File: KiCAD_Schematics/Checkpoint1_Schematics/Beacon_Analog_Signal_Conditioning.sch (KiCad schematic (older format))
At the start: 19 parts, among them Q1 Photo_NPN, U1 MCP6294, U1 MCP6546, U4 MCP6294

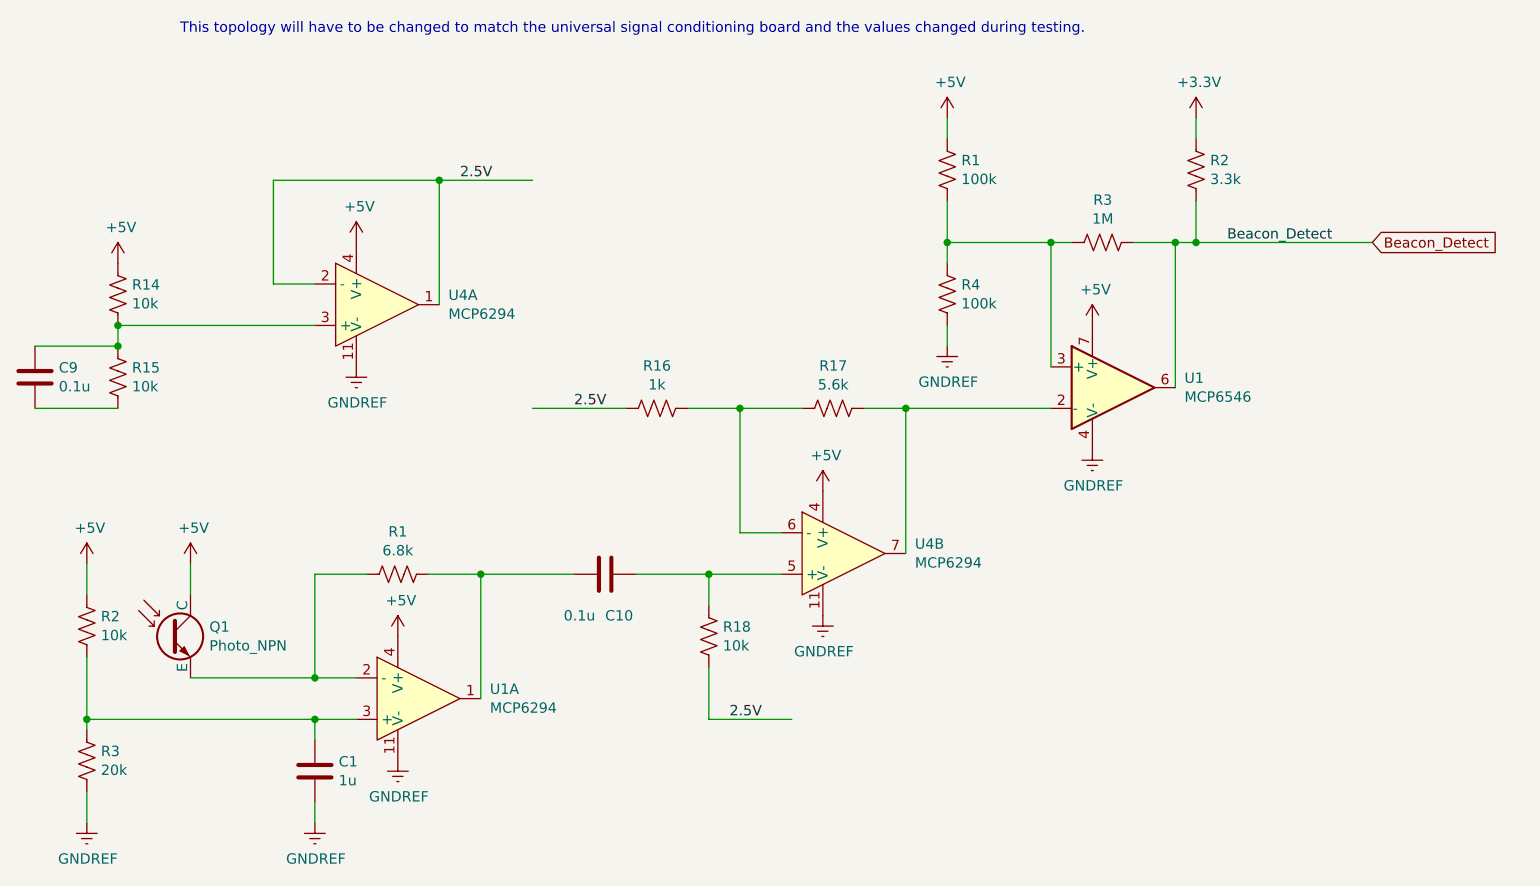
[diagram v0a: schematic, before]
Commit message: Update KiCAD schematic
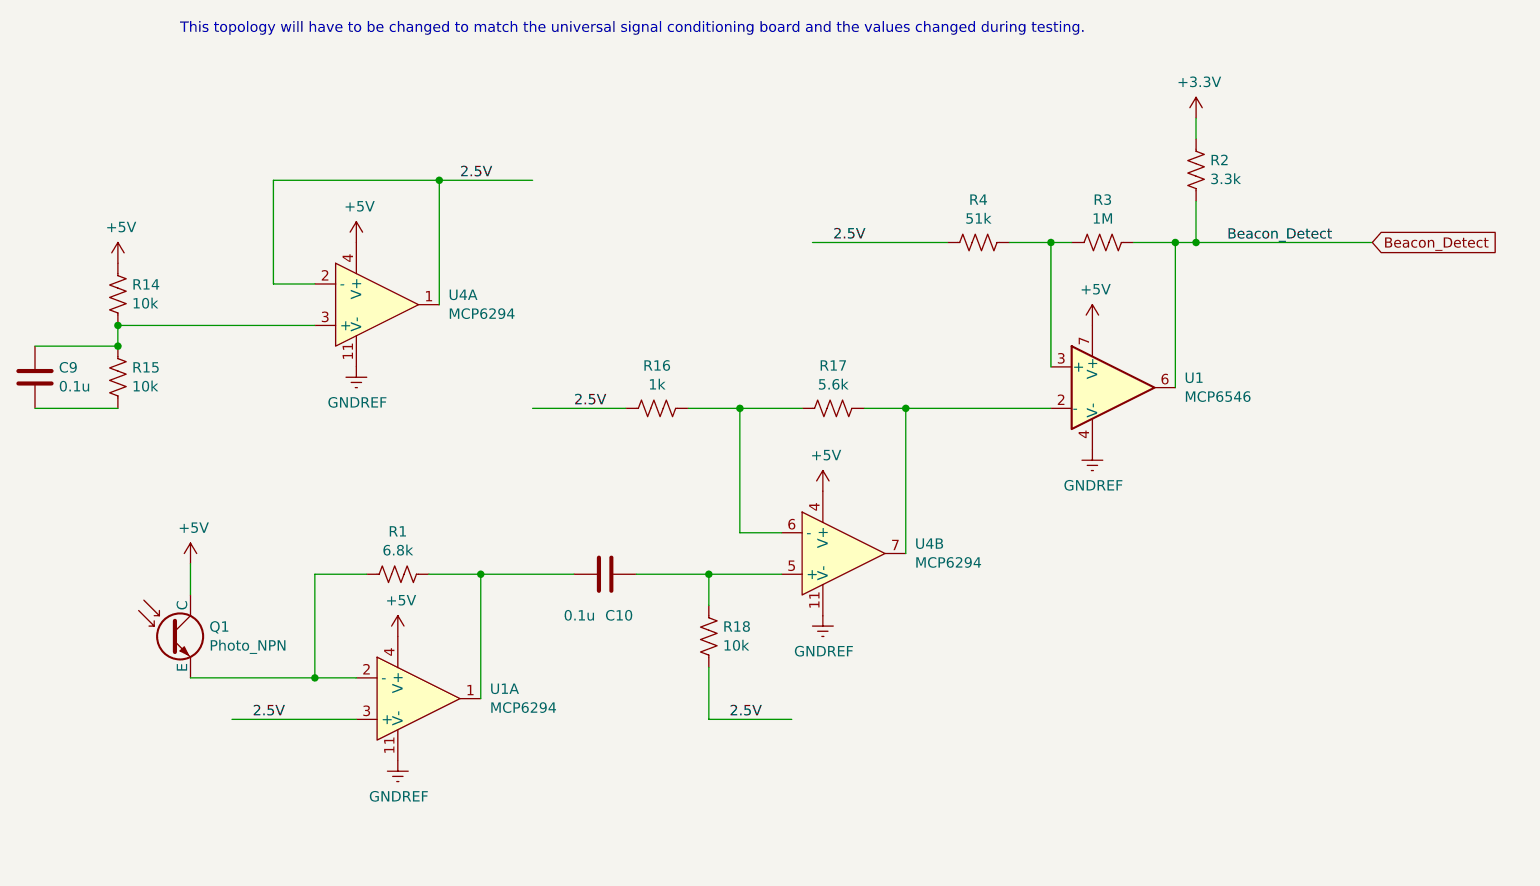
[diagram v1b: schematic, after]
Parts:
- removed C1: 1u, symbol ME218_BaseLib:Cap
- removed R1: 100k, symbol ME218_BaseLib:Res1
- removed R2: 10k, symbol ME218_BaseLib:Res1
- removed R3: 20k, symbol ME218_BaseLib:Res1
- R4: value 100k -> 51k
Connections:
- wire segments 51 -> 41
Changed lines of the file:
@@
 $Descr A4 11693 8268
 encoding utf-8
-Sheet 4 7
+Sheet 1 1
 Title "ME 218b Team 3 Project Schematic"
 Date ""
@@
 	1    0    0    -1
 $EndComp
-$Comp
-L power:+5V #PWR038
-U 1 1 61E4D0CB
-P 7100 2650
-F 0 "#PWR038" H 7100 2500 50  0001 C CNN
-F 1 "+5V" H 7115 2823 50  0000 C CNN
-F 2 "" H 7100 2650 50  0001 C CNN
-F 3 "" H 7100 2650 50  0001 C CNN
-	1    7100 2650
-	1    0    0    -1
-$EndComp
 Wire Wire Line
 	8000 3250 8200 3250
 Wire Wire Line
 	7600 3250 7700 3250
-Connection ~ 7600 3250
 Wire Wire Line
 	7600 3850 7600 3250
-Wire Wire Line
-	7100 3250 7100 3350
-Connection ~ 7100 3250
-Wire Wire Line
-	7100 3250 7600 3250
-Wire Wire Line
-	7100 3650 7100 3750
-Wire Wire Line
-	7100 3050 7100 3250
-Wire Wire Line
-	7100 2650 7100 2750
-$Comp
-L ME218_BaseLib:Res1 R4
-U 1 1 623811DC
-P 7100 3500
-F 0 "R4" H 7168 3546 50  0000 L CNN
-F 1 "100k" H 7168 3455 50  0000 L CNN
-F 2 "" V 7140 3490 50  0001 C CNN
-F 3 "" H 7100 3500 50  0001 C CNN
-	1    7100 3500
-	1    0    0    -1
-$EndComp
-$Comp
-L ME218_BaseLib:Res1 R1
-U 1 1 623811DB
-P 7100 2900
-F 0 "R1" H 7168 2946 50  0000 L CNN
-F 1 "100k" H 7168 2855 50  0000 L CNN
-F 2 "" V 7140 2890 50  0001 C CNN
-F 3 "" H 7100 2900 50  0001 C CNN
-	1    7100 2900
-	1    0    0    -1
-$EndComp
 $Comp
 L ME218_BaseLib:Res1 R3
@@
 $EndComp
 Wire Wire Line
-	4050 5550 4250 5550
-Connection ~ 4050 5550
-Wire Wire Line
-	4050 5650 4050 5550
-Wire Wire Line
-	4050 6050 4050 5950
-$Comp
-L ME218_BaseLib:Cap C1
-U 1 1 623811D4
-P 4050 5800
-F 0 "C1" H 4165 5846 50  0000 L CNN
-F 1 "1u" H 4165 5755 50  0000 L CNN
-F 2 "" H 4088 5650 50  0001 C CNN
-F 3 "" H 4050 5800 50  0001 C CNN
-	1    4050 5800
-	1    0    0    -1
-$EndComp
-Wire Wire Line
-	2950 5550 2950 5250
-Connection ~ 2950 5550
-Wire Wire Line
-	2950 5550 4050 5550
-Wire Wire Line
-	2950 5600 2950 5550
-Wire Wire Line
-	2950 5900 2950 6050
-Wire Wire Line
-	2950 4800 2950 4950
-$Comp
-L ME218_BaseLib:Res1 R3
-U 1 1 61DD96B1
-P 2950 5750
-F 0 "R3" H 3018 5796 50  0000 L CNN
-F 1 "20k" H 3018 5705 50  0000 L CNN
-F 2 "" V 2990 5740 50  0001 C CNN
-F 3 "" H 2950 5750 50  0001 C CNN
-	1    2950 5750
-	1    0    0    -1
-$EndComp
-$Comp
-L ME218_BaseLib:Res1 R2
-U 1 1 623811D2
-P 2950 5100
-F 0 "R2" H 3018 5146 50  0000 L CNN
-F 1 "10k" H 3018 5055 50  0000 L CNN
-F 2 "" V 2990 5090 50  0001 C CNN
-F 3 "" H 2950 5100 50  0001 C CNN
-	1    2950 5100
-	1    0    0    -1
-$EndComp
-$Comp
-L power:+5V #PWR01
-U 1 1 623811D0
-P 2950 4800
-F 0 "#PWR01" H 2950 4650 50  0001 C CNN
-F 1 "+5V" H 2965 4973 50  0000 C CNN
-F 2 "" H 2950 4800 50  0001 C CNN
-F 3 "" H 2950 4800 50  0001 C CNN
-	1    2950 4800
-	1    0    0    -1
-$EndComp
-Wire Wire Line
 	4600 4850 4850 4850
 Wire Wire Line
@@
 $EndComp
 $Comp
+L ME218_BaseLib:Photo_NPN Q1
+U 1 1 6238256B
+P 3350 5150
+F 0 "Q1" H 3541 5196 50  0000 L CNN
+F 1 "Photo_NPN" H 3541 5105 50  0000 L CNN
+F 2 "" H 3550 5250 50  0001 C CNN
+F 3 "" H 3350 5150 50  0001 C CNN
+	1    3350 5150
+	1    0    0    -1
+$EndComp
+$Comp
+L power:+5V #PWR02
+U 1 1 6238256A
+P 3450 4800
+F 0 "#PWR02" H 3450 4650 50  0001 C CNN
+F 1 "+5V" H 3465 4973 50  0000 C CNN
+F 2 "" H 3450 4800 50  0001 C CNN
+F 3 "" H 3450 4800 50  0001 C CNN
+	1    3450 4800
+	1    0    0    -1
+$EndComp
+Connection ~ 8300 3250
+Wire Wire Line
+	8300 3250 9150 3250
+Text Label 8450 3250 0    49   ~ 0
+Beacon_Detect
+Text GLabel 9150 3250 2    49   Input ~ 0
+Beacon_Detect
+Text Notes 3400 2250 0    50   ~ 0
+This topology will have to be changed to match the universal signal conditioning board and the values changed during testing.
+$Comp
+L power:GNDREF #PWR046
+U 1 1 623EC563
+P 4450 5750
+F 0 "#PWR046" H 4450 5500 50  0001 C CNN
+F 1 "GNDREF" H 4455 5577 50  0000 C CNN
+F 2 "" H 4450 5750 50  0001 C CNN
+F 3 "" H 4450 5750 50  0001 C CNN
+	1    4450 5750
+	1    0    0    -1
+$EndComp
+$Comp
+L power:GNDREF #PWR045
+U 1 1 623EC85B
+P 6500 5050
+F 0 "#PWR045" H 6500 4800 50  0001 C CNN
+F 1 "GNDREF" H 6505 4877 50  0000 C CNN
+F 2 "" H 6500 5050 50  0001 C CNN
+F 3 "" H 6500 5050 50  0001 C CNN
+	1    6500 5050
+	1    0    0    -1
+$EndComp
+$Comp
+L power:GNDREF #PWR043
+U 1 1 623ED00D
+P 7800 4250
+F 0 "#PWR043" H 7800 4000 50  0001 C CNN
+F 1 "GNDREF" H 7805 4077 50  0000 C CNN
+F 2 "" H 7800 4250 50  0001 C CNN
+F 3 "" H 7800 4250 50  0001 C CNN
+	1    7800 4250
+	1    0    0    -1
+$EndComp
+$Comp
+L power:GNDREF #PWR042
+U 1 1 623EEBCB
+P 4250 3850
+F 0 "#PWR042" H 4250 3600 50  0001 C CNN
+F 1 "GNDREF" H 4255 3677 50  0000 C CNN
+F 2 "" H 4250 3850 50  0001 C CNN
+F 3 "" H 4250 3850 50  0001 C CNN
+	1    4250 3850
+	1    0    0    -1
+$EndComp
+Text Label 6550 3250 0    50   ~ 0
+2.5V
+$Comp
+L ME218_BaseLib:Res1 R4
+U 1 1 6212ADA5
+P 7250 3250
+F 0 "R4" V 7045 3250 50  0000 C CNN
+F 1 "51k" V 7136 3250 50  0000 C CNN
+F 2 "" V 7290 3240 50  0001 C CNN
+F 3 "" H 7250 3250 50  0001 C CNN
+	1    7250 3250
+	0    1    1    0
+$EndComp
+Wire Wire Line
+	6450 3250 7100 3250
+Wire Wire Line
+	7400 3250 7600 3250
+Connection ~ 7600 3250
+Text Label 3750 5550 0    50   ~ 0
+2.5V
+$Comp
 L ME218_BaseLib:MCP6294 U1
 U 1 1 6238256C
@@
 	1    0    0    -1
 $EndComp
-$Comp
-L ME218_BaseLib:Photo_NPN Q1
-U 1 1 6238256B
-P 3350 5150
-F 0 "Q1" H 3541 5196 50  0000 L CNN
-F 1 "Photo_NPN" H 3541 5105 50  0000 L CNN
-F 2 "" H 3550 5250 50  0001 C CNN
-F 3 "" H 3350 5150 50  0001 C CNN
-	1    3350 5150
-	1    0    0    -1
-$EndComp
-$Comp
-L power:+5V #PWR02
-U 1 1 6238256A
-P 3450 4800
-F 0 "#PWR02" H 3450 4650 50  0001 C CNN
-F 1 "+5V" H 3465 4973 50  0000 C CNN
-F 2 "" H 3450 4800 50  0001 C CNN
-F 3 "" H 3450 4800 50  0001 C CNN
-	1    3450 4800
-	1    0    0    -1
-$EndComp
-Connection ~ 8300 3250
-Wire Wire Line
-	8300 3250 9150 3250
-Text Label 8450 3250 0    49   ~ 0
-Beacon_Detect
-Text GLabel 9150 3250 2    49   Input ~ 0
-Beacon_Detect
-Text Notes 3400 2250 0    50   ~ 0
-This topology will have to be changed to match the universal signal conditioning board and the values changed during testing.
-$Comp
-L power:GNDREF #PWR047
-U 1 1 623E673A
-P 2950 6050
-F 0 "#PWR047" H 2950 5800 50  0001 C CNN
-F 1 "GNDREF" H 2955 5877 50  0000 C CNN
-F 2 "" H 2950 6050 50  0001 C CNN
-F 3 "" H 2950 6050 50  0001 C CNN
-	1    2950 6050
-	1    0    0    -1
-$EndComp
-$Comp
-L power:GNDREF #PWR048
-U 1 1 623EC209
-P 4050 6050
-F 0 "#PWR048" H 4050 5800 50  0001 C CNN
-F 1 "GNDREF" H 4055 5877 50  0000 C CNN
-F 2 "" H 4050 6050 50  0001 C CNN
-F 3 "" H 4050 6050 50  0001 C CNN
-	1    4050 6050
-	1    0    0    -1
-$EndComp
-$Comp
-L power:GNDREF #PWR046
-U 1 1 623EC563
-P 4450 5750
-F 0 "#PWR046" H 4450 5500 50  0001 C CNN
-F 1 "GNDREF" H 4455 5577 50  0000 C CNN
-F 2 "" H 4450 5750 50  0001 C CNN
-F 3 "" H 4450 5750 50  0001 C CNN
-	1    4450 5750
-	1    0    0    -1
-$EndComp
-$Comp
-L power:GNDREF #PWR045
-U 1 1 623EC85B
-P 6500 5050
-F 0 "#PWR045" H 6500 4800 50  0001 C CNN
-F 1 "GNDREF" H 6505 4877 50  0000 C CNN
-F 2 "" H 6500 5050 50  0001 C CNN
-F 3 "" H 6500 5050 50  0001 C CNN
-	1    6500 5050
-	1    0    0    -1
-$EndComp
-$Comp
-L power:GNDREF #PWR043
-U 1 1 623ED00D
-P 7800 4250
-F 0 "#PWR043" H 7800 4000 50  0001 C CNN
-F 1 "GNDREF" H 7805 4077 50  0000 C CNN
-F 2 "" H 7800 4250 50  0001 C CNN
-F 3 "" H 7800 4250 50  0001 C CNN
-	1    7800 4250
-	1    0    0    -1
-$EndComp
-$Comp
-L power:GNDREF #PWR041
-U 1 1 623EE235
-P 7100 3750
-F 0 "#PWR041" H 7100 3500 50  0001 C CNN
-F 1 "GNDREF" H 7105 3577 50  0000 C CNN
-F 2 "" H 7100 3750 50  0001 C CNN
-F 3 "" H 7100 3750 50  0001 C CNN
-	1    7100 3750
-	1    0    0    -1
-$EndComp
-$Comp
-L power:GNDREF #PWR042
-U 1 1 623EEBCB
-P 4250 3850
-F 0 "#PWR042" H 4250 3600 50  0001 C CNN
-F 1 "GNDREF" H 4255 3677 50  0000 C CNN
-F 2 "" H 4250 3850 50  0001 C CNN
-F 3 "" H 4250 3850 50  0001 C CNN
-	1    4250 3850
-	1    0    0    -1
-$EndComp
+Wire Wire Line
+	3650 5550 4250 5550
 $EndSCHEMATC
